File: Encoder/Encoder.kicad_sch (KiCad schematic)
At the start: 10 parts, among them J1 Conn_01x04, U1 AS5600

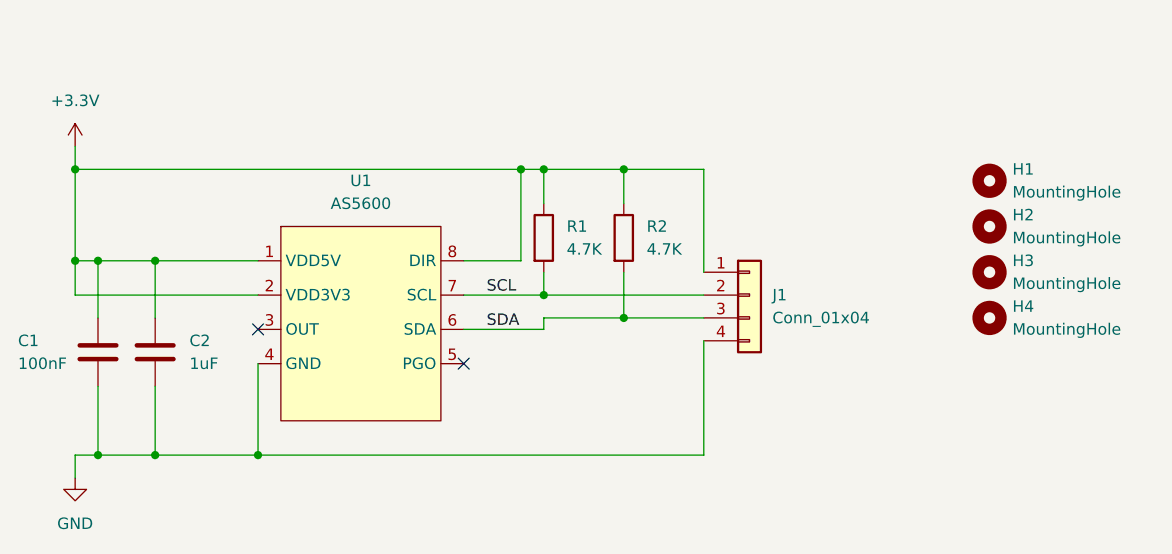
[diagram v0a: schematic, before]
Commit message: Add switch for CW/CCW control
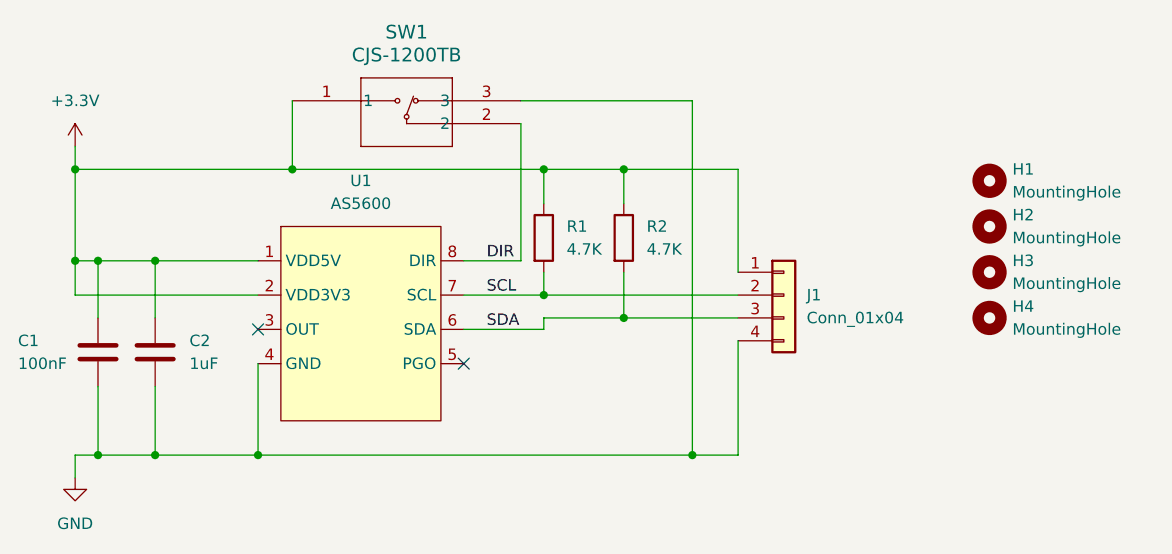
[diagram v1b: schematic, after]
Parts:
- added SW1: CJS-1200TB, RoboMaster:CJS-1200B_NDC, symbol RoboMaster:CJS-1200TB
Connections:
- net +3.3V: now also SW1.1; no longer U1.8 (DIR)
- net GND: now also SW1.3
- new net DIR: SW1.2, U1.8 (DIR)
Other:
- moved on the sheet: J1
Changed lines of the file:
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@@
-	)
-	(junction
-		(at 93.98 48.26)
-		(diameter 0)
-		(color 0 0 0 0)
 	)
 	(junction
@@
 	)
 	(junction
+		(at 113.03 80.01)
+		(diameter 0)
+		(color 0 0 0 0)
+	)
+	(junction
 		(at 44.45 58.42)
+		(diameter 0)
+		(color 0 0 0 0)
+	)
+	(junction
+		(at 68.58 48.26)
 		(diameter 0)
 		(color 0 0 0 0)
@@
 	(wire
 		(pts
-			(xy 114.3 67.31) (xy 114.3 80.01)
+			(xy 118.11 67.31) (xy 118.11 80.01)
 		)
 		(stroke
@@
 	(wire
 		(pts
-			(xy 105.41 48.26) (xy 114.3 48.26)
-		)
-		(stroke
-			(width 0)
-			(type default)
-		)
-	)
-	(wire
-		(pts
-			(xy 44.45 48.26) (xy 93.98 48.26)
+			(xy 105.41 48.26) (xy 118.11 48.26)
+		)
+		(stroke
+			(width 0)
+			(type default)
+		)
+	)
+	(wire
+		(pts
+			(xy 44.45 48.26) (xy 68.58 48.26)
+		)
+		(stroke
+			(width 0)
+			(type default)
+		)
+	)
+	(wire
+		(pts
+			(xy 68.58 40.64) (xy 68.58 48.26)
 		)
 		(stroke
@@
 	(wire
 		(pts
-			(xy 64.77 80.01) (xy 114.3 80.01)
+			(xy 64.77 80.01) (xy 113.03 80.01)
 		)
 		(stroke
@@
 	(wire
 		(pts
-			(xy 96.52 62.23) (xy 114.3 62.23)
+			(xy 96.52 62.23) (xy 118.11 62.23)
 		)
 		(stroke
@@
 	(wire
 		(pts
-			(xy 93.98 58.42) (xy 93.98 48.26)
-		)
-		(stroke
-			(width 0)
-			(type default)
-		)
-	)
-	(wire
-		(pts
-			(xy 114.3 48.26) (xy 114.3 59.69)
+			(xy 118.11 48.26) (xy 118.11 59.69)
 		)
 		(stroke
@@
 	(wire
 		(pts
-			(xy 105.41 64.77) (xy 114.3 64.77)
+			(xy 105.41 64.77) (xy 118.11 64.77)
 		)
 		(stroke
@@
 	(wire
 		(pts
+			(xy 113.03 80.01) (xy 118.11 80.01)
+		)
+		(stroke
+			(width 0)
+			(type default)
+		)
+	)
+	(wire
+		(pts
 			(xy 96.52 66.04) (xy 96.52 64.77)
 		)
@@
 	(wire
 		(pts
+			(xy 93.98 43.18) (xy 93.98 58.42)
+		)
+		(stroke
+			(width 0)
+			(type default)
+		)
+	)
+	(wire
+		(pts
 			(xy 44.45 80.01) (xy 44.45 82.55)
 		)
@@
 	(wire
 		(pts
-			(xy 93.98 48.26) (xy 96.52 48.26)
+			(xy 93.98 40.64) (xy 113.03 40.64)
 		)
 		(stroke
@@
 		(pts
 			(xy 44.45 58.42) (xy 46.99 58.42)
+		)
+		(stroke
+			(width 0)
+			(type default)
+		)
+	)
+	(wire
+		(pts
+			(xy 113.03 40.64) (xy 113.03 80.01)
+		)
+		(stroke
+			(width 0)
+			(type default)
+		)
+	)
+	(wire
+		(pts
+			(xy 68.58 48.26) (xy 96.52 48.26)
 		)
 		(stroke
@@
 	(label "SDA"
 		(at 90.17 66.04 0)
+		(fields_autoplaced yes)
+		(effects
+			(font
+				(size 1.27 1.27)
+			)
+			(justify left bottom)
+		)
+	)
+	(label "DIR"
+		(at 90.17 58.42 0)
 		(fields_autoplaced yes)
 		(effects
@@
 	(symbol
 		(lib_id "Connector_Generic:Conn_01x04")
-		(at 119.38 62.23 0)
+		(at 123.19 62.23 0)
 		(unit 1)
 		(exclude_from_sim no)
@@
 		(fields_autoplaced yes)
 		(property "Reference" "J1"
-			(at 121.92 62.2299 0)
+			(at 125.73 62.2299 0)
 			(effects
 				(font
@@
 		)
 		(property "Value" "Conn_01x04"
-			(at 121.92 64.7699 0)
+			(at 125.73 64.7699 0)
 			(effects
 				(font
@@
 		)
 		(property "Footprint" "Connector_JST:JST_GH_SM04B-GHS-TB_1x04-1MP_P1.25mm_Horizontal"
-			(at 118.364 55.118 0)
+			(at 122.174 55.118 0)
 			(effects
 				(font
@@
 		)
 		(property "Datasheet" "~"
-			(at 119.38 62.23 0)
+			(at 123.19 62.23 0)
 			(effects
 				(font
@@
 		)
 		(property "Description" "Generic connector, single row, 01x04, script generated (kicad-library-utils/schlib/autogen/connector/)"
-			(at 118.872 56.896 0)
+			(at 122.682 56.896 0)
 			(effects
 				(font
@@
 					(unit 1)
 				)
+			)
+		)
+	)
+	(symbol
+		(lib_id "RoboMaster:CJS-1200TB")
+		(at 68.58 40.64 0)
+		(unit 1)
+		(exclude_from_sim no)
+		(in_bom yes)
+		(on_board yes)
+		(dnp no)
+		(fields_autoplaced yes)
+		(property "Reference" "SW1"
+			(at 81.28 33.02 0)
+			(effects
+				(font
+					(size 1.524 1.524)
+				)
+			)
+		)
+		(property "Value" "CJS-1200TB"
+			(at 81.28 35.56 0)
+			(effects
+				(font
+					(size 1.524 1.524)
+				)
+			)
+		)
+		(property "Footprint" "RoboMaster:CJS-1200B_NDC"
+			(at 83.058 48.006 0)
+			(effects
+				(font
+					(size 1.27 1.27)
+					(italic yes)
+				)
+				(hide yes)
+			)
+		)
+		(property "Datasheet" "CJS-1200TB"
+			(at 83.058 50.546 0)
+			(effects
+				(font
+					(size 1.27 1.27)
+					(italic yes)
+				)
+				(hide yes)
+			)
+		)
+		(property "Description" ""
+			(at 68.58 40.64 0)
+			(effects
+				(font
+					(size 1.27 1.27)
+				)
+				(hide yes)
+			)
+		)
+		(pin "1"
+		)
+		(pin "3"
+		)
+		(pin "2"
+		)
+		(instances
+			(project ""
+				(path "/77501ba7-0423-44f5-b0cd-3d1dd0a587ed"
+					(reference "SW1")
+					(unit 1)
+				)
